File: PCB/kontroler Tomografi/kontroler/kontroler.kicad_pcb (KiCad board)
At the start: 4 copper layers, 67.5 x 76 mm, 23 parts, among them J1 In_VCCS, J2 Out_Switch, J3 In_Switch, J4 V_In, U1 AD620, U2 ESP32-S3-DevKitC, U4 L7805

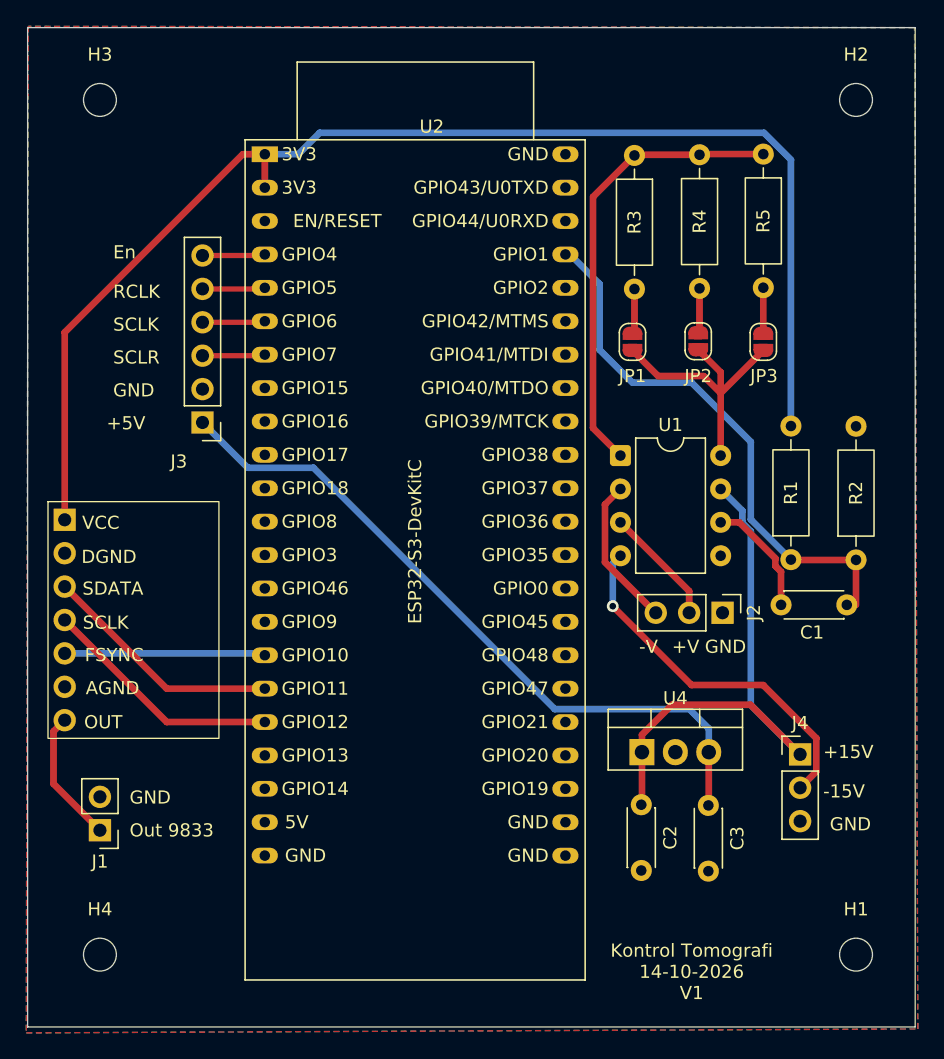
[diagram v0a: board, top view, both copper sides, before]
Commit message: PCB kontroler tomografi V2
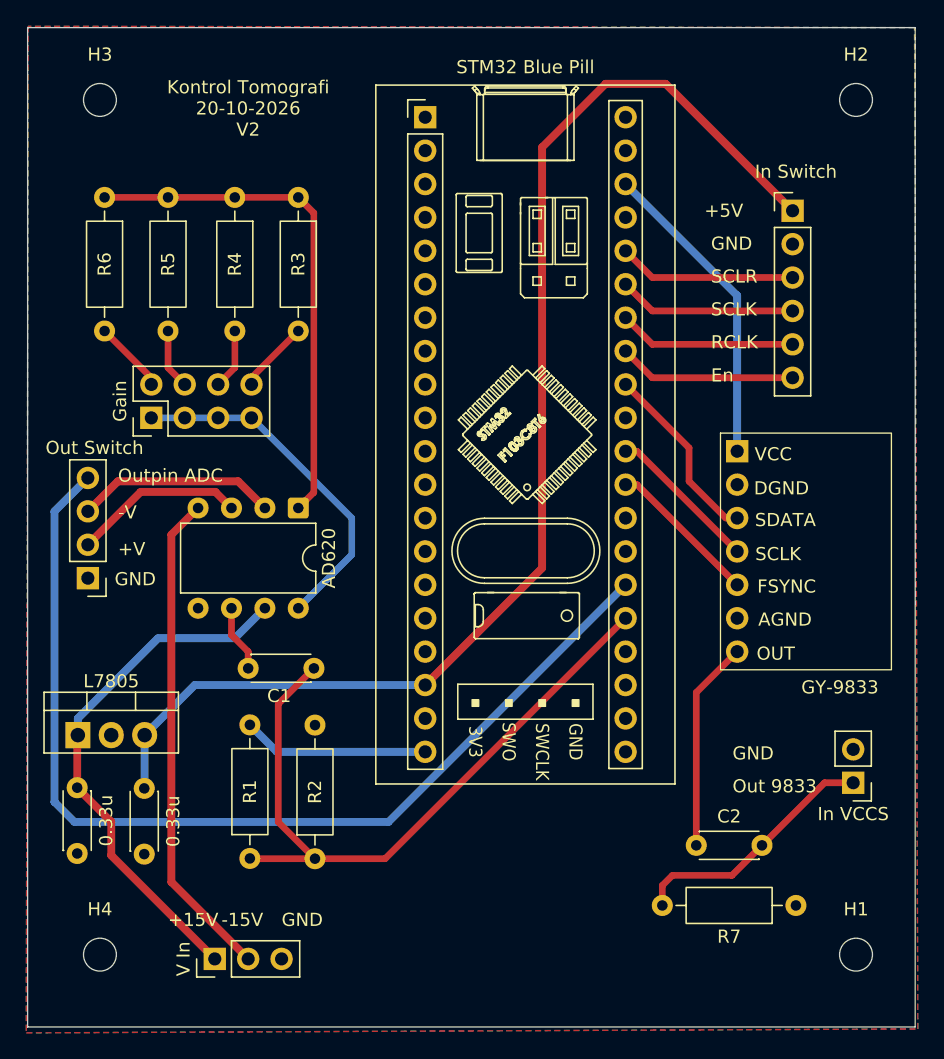
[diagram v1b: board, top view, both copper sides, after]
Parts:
- removed J4: V_In, Connector_PinHeader_2.54mm:PinHeader_1x03_P2.54mm_Vertical
- removed JP1: 100G, Jumper:SolderJumper-2_P1.3mm_Open_RoundedPad1.0x1.5mm
- removed JP2: 10G, Jumper:SolderJumper-2_P1.3mm_Open_RoundedPad1.0x1.5mm
- removed JP3: 1G, Jumper:SolderJumper-2_P1.3mm_Open_RoundedPad1.0x1.5mm
- removed U2: ESP32-S3-DevKitC, PCM_Espressif:ESP32-S3-DevKitC
- added C2: C, Capacitor_THT:C_Disc_D4.3mm_W1.9mm_P5.00mm, F.Cu at (130.8, 107.2)
- added Gain: Conn_02x04_Odd_Even, Connector_PinHeader_2.54mm:PinHeader_2x04_P2.54mm_Vertical, F.Cu at (89.4, 74.7)
- added Out Switch: Out_Switch, Connector_PinHeader_2.54mm:PinHeader_1x04_P2.54mm_Vertical, F.Cu at (84.6, 86.9)
- added R6: 49.4k, Resistor_THT:R_Axial_DIN0207_L6.3mm_D2.5mm_P10.16mm_Horizontal, F.Cu at (85.9, 57.9)
- added R7: R, Resistor_THT:R_Axial_DIN0207_L6.3mm_D2.5mm_P10.16mm_Horizontal, F.Cu at (138.4, 111.8)
- added STM32 Blue Pill: YAAJ_BluePill, Library:YAAJ_BluePill_1, F.Cu at (110.2, 51.8)
- In Switch: renamed from J3
- In VCCS: renamed from J1
- R3: value 494 -> 499
- R4: value 4.94k -> 5.94k
- V In: renamed from J2; value Out_Switch -> V_In
- moved In VCCS 57.4 mm to (142.8, 102.4)
- moved U3 51.4 mm to (142.9, 86.1)
- moved In Switch 47.7 mm to (138.2, 58.9), turned to 0 degrees
- moved R1 47.0 mm to (96.9, 108.2)
- moved R2 47.0 mm to (101.9, 108.2)
- moved V In 46.7 mm to (94.2, 115.8), turned to 90 degrees
- moved R5 45.4 mm to (90.7, 57.9)
- moved 0.33u 42.9 mm to (88.9, 102.9)
- moved 0.33u 42.9 mm to (83.8, 102.8)
- moved L7805 42.9 mm to (83.8, 98.8)
- moved C1 40.8 mm to (96.8, 93.7)
- moved R4 35.5 mm to (95.8, 57.9)
- moved R3 25.8 mm to (100.6, 57.9)
- moved AD620 24.8 mm to (100.6, 81.5), turned to -90 degrees
- renumbered C2 to 0.33u, C3 to 0.33u, U1 to AD620, U4 to L7805
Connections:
- In Switch pad 4: /SCLK -> /SCLK2
- In VCCS pad 1: /Out 9833 -> /Out HPF
- U3 pad 3: /GPIO11 -> /SDATA
- U3 pad 4: /GPIO12 -> /SCLK1
- U3 pad 5: /GPIO10 -> /FSYNC
- V In pad 1: GND -> +15V
- V In pad 2: /+V -> -15V
- V In pad 3: /-V -> GND
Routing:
- net /Out pin ADC: track 0.00 -> 77.2 mm
- net +3.3V: track 99.4 -> 38.0 mm
- net +5V: track 54.0 -> 96.6 mm
- net /Out HPF: track 0.00 -> 19.3 mm
- net /GPIO12: track 18.4 -> 0.00 mm
- net /GPIO11: track 18.4 -> 0.00 mm
- net /GPIO10: track 15.3 -> 0.00 mm
- net /SDATA: track 0.00 -> 14.2 mm
- net /SCLK2: track 0.00 -> 13.5 mm
- net /SCLK1: track 0.00 -> 11.6 mm
- net /FSYNC: track 0.00 -> 11.6 mm
- net /Out ADC: track 41.7 -> 52.9 mm
- net -15V: track 28.0 -> 37.6 mm, vias 1 -> 0
- net /SCLR: track 4.77 -> 13.5 mm
- net /RCLK: track 4.77 -> 13.5 mm
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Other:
- board text added: "GY-9833"
- board text added: "Kontrol Tomografi 20-10-2026 V2"
- board text added: "Outpin ADC"
- board text removed: "Kontrol Tomografi 14-10-2026 V1"

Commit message: PCB kontroler tomografi V2.1
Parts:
- removed 0.33u: 0.33u, Capacitor_THT:C_Disc_D4.3mm_W1.9mm_P5.00mm
- removed 0.33u: 0.1u, Capacitor_THT:C_Disc_D4.3mm_W1.9mm_P5.00mm
- removed L7805: L7805, Package_TO_SOT_THT:TO-220-3_Vertical
- added 5V: V 5V, Connector_PinHeader_2.54mm:PinHeader_1x02_P2.54mm_Vertical, F.Cu at (95.5, 113.8)
- InSwitch: renamed from In Switch
- moved V In 22.3 mm to (84.6, 95.8), turned to 0 degrees
- moved C1 1.30 mm to (95.5, 94.0)
- moved R1 1.30 mm to (95.6, 107.9)
- moved R2 1.30 mm to (100.6, 108.0)
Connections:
- net -15V renamed -5V
- AD620 pad 7: +15V -> +5VA
- InSwitch pad 1: +5V -> +5VA
- V In pad 1: +15V -> +5VA
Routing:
- net +5VA: track 0.00 -> 123.3 mm
- net +5V: track 96.6 -> 23.9 mm, vias 0 -> 1
- net +15V: track 40.3 -> 0.00 mm
- net -5V: track 37.6 -> 20.2 mm
- net +3.3V: track 38.0 -> 39.4 mm
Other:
- board text added: "+5VC"
- board text added: "-5V"
- board text added: "Kontrol Tomografi 21-10-2026 V2.1"
- board text removed: "+15V"
- board text removed: "-15V"
- board text removed: "Kontrol Tomografi 20-10-2026 V2"
